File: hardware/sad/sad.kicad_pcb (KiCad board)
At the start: 2 copper layers, 69 parts, among them IC1 LP5012RUKR, J1 USB_C_Receptacle_USB2.0_16P, U1 ATtiny1616-M, U2 MCP73831-2-OT

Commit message: switches updated; border
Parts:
- moved C4 1.90 mm to (158.0, 83.8), turned to -90 degrees
- moved C3 1.84 mm to (147.8, 83.7), turned to -90 degrees
- moved R8 0.90 mm to (158.0, 81.2), turned to 90 degrees
- moved R9 0.90 mm to (147.8, 81.2), turned to 90 degrees
- moved C1 0.79 mm to (168.8, 83.3)
- moved C2 0.79 mm to (167.8, 83.3)
- moved R10 0.79 mm to (174.2, 81.9)
- moved R11 0.79 mm to (174.2, 84.2)
- moved R2 0.79 mm to (169.2, 85.5)
- moved U1 0.79 mm to (171.5, 83.2)
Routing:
- net Net-(S2-NO_1): track 2.17 -> 0.00 mm
- net /SW2: track 1.01 -> 0.00 mm
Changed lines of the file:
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@@
 	(footprint "Resistor_SMD:R_0402_1005Metric_Pad0.72x0.64mm_HandSolder"
 		(layer "F.Cu")
-		(at 158.75 80.75 180)
+		(at 158 81.25 90)
 		(descr "Resistor SMD 0402 (1005 Metric), square (rectangular) end terminal, IPC-7351 nominal with elongated pad for handsoldering. (Body size source: IPC-SM-782 page 72, https://www.pcb-3d.com/wordpress/wp-content/uploads/ipc-sm-782a_amendment_1_and_2.pdf)")
 		(tags "resistor handsolder")
 		(property "Reference" "R8"
-			(at -2 0 0)
+			(at 0 1.5 180)
 			(layer "F.SilkS")
 			(effects
@@
 		)
 		(property "Value" "1k"
-			(at 0 1.17 0)
+			(at 0 1.17 90)
 			(layer "F.Fab")
 			(effects
@@
 		)
 		(property "Datasheet" ""
-			(at 0 0 0)
+			(at 0 0 90)
 			(layer "F.Fab")
 			(hide yes)
@@
 		)
 		(property "Description" "Resistor"
-			(at 0 0 0)
+			(at 0 0 90)
 			(layer "F.Fab")
 			(hide yes)
@@
 		)
 		(property "KiLib_Generator" "SMD_2terminal_chip_molded"
-			(at 0 0 0)
+			(at 0 0 90)
 			(layer "F.SilkS")
 			(hide yes)
@@
 		(duplicate_pad_numbers_are_jumpers no)
 		(fp_line
-			(start -0.167621 0.38)
-			(end 0.167621 0.38)
+			(start -0.167621 -0.38)
+			(end 0.167621 -0.38)
 			(stroke
 				(width 0.12)
@@
 		)
 		(fp_line
-			(start -0.167621 -0.38)
-			(end 0.167621 -0.38)
+			(start -0.167621 0.38)
+			(end 0.167621 0.38)
 			(stroke
 				(width 0.12)
@@
 		)
 		(fp_text user "${REFERENCE}"
-			(at 0 0 0)
+			(at 0 0 90)
 			(layer "F.Fab")
 			(effects
@@
 		)
 		(pad "1" smd roundrect
-			(at -0.5975 0 180)
+			(at -0.5975 0 90)
 			(size 0.715 0.64)
 			(layers "F.Cu" "F.Mask" "F.Paste")
@@
 		)
 		(pad "2" smd roundrect
-			(at 0.5975 0 180)
+			(at 0.5975 0 90)
 			(size 0.715 0.64)
 			(layers "F.Cu" "F.Mask" "F.Paste")
@@
 	(footprint "Capacitor_SMD:C_0402_1005Metric_Pad0.74x0.62mm_HandSolder"
 		(layer "F.Cu")
-		(at 168 83.5675 90)
+		(at 168.75 83.3175 90)
 		(descr "Capacitor SMD 0402 (1005 Metric), square (rectangular) end terminal, IPC-7351 nominal with elongated pad for handsoldering. (Body size source: IPC-SM-782 page 76, https://www.pcb-3d.com/wordpress/wp-content/uploads/ipc-sm-782a_amendment_1_and_2.pdf)")
 		(tags "capacitor handsolder")
@@
 	(footprint "Resistor_SMD:R_0402_1005Metric_Pad0.72x0.64mm_HandSolder"
 		(layer "F.Cu")
-		(at 173.5 82.1525 -90)
+		(at 174.25 81.9025 -90)
 		(descr "Resistor SMD 0402 (1005 Metric), square (rectangular) end terminal, IPC-7351 nominal with elongated pad for handsoldering. (Body size source: IPC-SM-782 page 72, https://www.pcb-3d.com/wordpress/wp-content/uploads/ipc-sm-782a_amendment_1_and_2.pdf)")
 		(tags "resistor handsolder")
@@
 	(footprint "Package_DFN_QFN:VQFN-20-1EP_3x3mm_P0.4mm_EP1.7x1.7mm"
 		(layer "F.Cu")
-		(at 170.75 83.5)
+		(at 171.5 83.25)
 		(descr "VQFN, 20 Pin (http://ww1.microchip.com/downloads/en/DeviceDoc/20%20Lead%20VQFN%203x3x0_9mm_1_7EP%20U2B%20C04-21496a.pdf)")
 		(tags "VQFN NoLead")
@@
 	(footprint "Resistor_SMD:R_0402_1005Metric_Pad0.72x0.64mm_HandSolder"
 		(layer "F.Cu")
-		(at 173.5 84.5 90)
+		(at 174.25 84.25 90)
 		(descr "Resistor SMD 0402 (1005 Metric), square (rectangular) end terminal, IPC-7351 nominal with elongated pad for handsoldering. (Body size source: IPC-SM-782 page 72, https://www.pcb-3d.com/wordpress/wp-content/uploads/ipc-sm-782a_amendment_1_and_2.pdf)")
 		(tags "resistor handsolder")
@@
 	(footprint "Capacitor_SMD:C_0402_1005Metric_Pad0.74x0.62mm_HandSolder"
 		(layer "F.Cu")
-		(at 158.75 82 180)
+		(at 158 83.75 -90)
 		(descr "Capacitor SMD 0402 (1005 Metric), square (rectangular) end terminal, IPC-7351 nominal with elongated pad for handsoldering. (Body size source: IPC-SM-782 page 76, https://www.pcb-3d.com/wordpress/wp-content/uploads/ipc-sm-782a_amendment_1_and_2.pdf)")
 		(tags "capacitor handsolder")
 		(property "Reference" "C4"
-			(at 0.25 -1.25 0)
+			(at 0 -1.25 180)
 			(layer "F.SilkS")
 			(effects
@@
 		)
 		(property "Value" "10nF"
-			(at 0 1.16 0)
+			(at 0 1.16 90)
 			(layer "F.Fab")
 			(effects
@@
 		)
 		(property "Datasheet" ""
-			(at 0 0 0)
+			(at 0 0 90)
 			(layer "F.Fab")
 			(hide yes)
@@
 		)
 		(property "Description" "Unpolarized capacitor"
-			(at 0 0 0)
+			(at 0 0 90)
 			(layer "F.Fab")
 			(hide yes)
@@
 		)
 		(property "KiLib_Generator" "SMD_2terminal_chip_molded"
-			(at 0 0 0)
+			(at 0 0 90)
 			(layer "F.SilkS")
 			(hide yes)
@@
 		)
 		(fp_text user "${REFERENCE}"
-			(at 0 0 0)
+			(at 0 0 90)
 			(layer "F.Fab")
 			(effects
@@
 		)
 		(pad "1" smd roundrect
-			(at -0.5675 0 180)
+			(at -0.5675 0 270)
 			(size 0.735 0.62)
 			(layers "F.Cu" "F.Mask" "F.Paste")
@@
 		)
 		(pad "2" smd roundrect
-			(at 0.5675 0 180)
+			(at 0.5675 0 270)
 			(size 0.735 0.62)
 			(layers "F.Cu" "F.Mask" "F.Paste")
@@
 	(footprint "Resistor_SMD:R_0402_1005Metric_Pad0.72x0.64mm_HandSolder"
 		(layer "F.Cu")
-		(at 148.5 80.75)
+		(at 147.75 81.25 90)
 		(descr "Resistor SMD 0402 (1005 Metric), square (rectangular) end terminal, IPC-7351 nominal with elongated pad for handsoldering. (Body size source: IPC-SM-782 page 72, https://www.pcb-3d.com/wordpress/wp-content/uploads/ipc-sm-782a_amendment_1_and_2.pdf)")
 		(tags "resistor handsolder")
 		(property "Reference" "R9"
-			(at 2 0.25 0)
+			(at 0 1.5 180)
 			(layer "F.SilkS")
 			(effects
@@
 		)
 		(property "Value" "1k"
-			(at 0 1.17 0)
+			(at 0 1.17 90)
 			(layer "F.Fab")
 			(effects
@@
 		)
 		(property "Datasheet" ""
-			(at 0 0 0)
+			(at 0 0 90)
 			(layer "F.Fab")
 			(hide yes)
@@
 		)
 		(property "Description" "Resistor"
-			(at 0 0 0)
+			(at 0 0 90)
 			(layer "F.Fab")
 			(hide yes)
@@
 		)
 		(property "KiLib_Generator" "SMD_2terminal_chip_molded"
-			(at 0 0 0)
+			(at 0 0 90)
 			(layer "F.SilkS")
 			(hide yes)
@@
 		)
 		(fp_text user "${REFERENCE}"
-			(at 0 0 0)
+			(at 0 0 90)
 			(layer "F.Fab")
 			(effects
@@
 		)
 		(pad "1" smd roundrect
-			(at -0.5975 0)
+			(at -0.5975 0 90)
 			(size 0.715 0.64)
 			(layers "F.Cu" "F.Mask" "F.Paste")
@@
 		)
 		(pad "2" smd roundrect
-			(at 0.5975 0)
+			(at 0.5975 0 90)
 			(size 0.715 0.64)
 			(layers "F.Cu" "F.Mask" "F.Paste")
@@
 	(footprint "Capacitor_SMD:C_0402_1005Metric_Pad0.74x0.62mm_HandSolder"
 		(layer "F.Cu")
-		(at 167 83.5675 -90)
+		(at 167.75 83.3175 -90)
 		(descr "Capacitor SMD 0402 (1005 Metric), square (rectangular) end terminal, IPC-7351 nominal with elongated pad for handsoldering. (Body size source: IPC-SM-782 page 76, https://www.pcb-3d.com/wordpress/wp-content/uploads/ipc-sm-782a_amendment_1_and_2.pdf)")
 		(tags "capacitor handsolder")
@@
 	(footprint "Resistor_SMD:R_0402_1005Metric_Pad0.72x0.64mm_HandSolder"
 		(layer "F.Cu")
-		(at 168.4 85.75 180)
+		(at 169.15 85.5 180)
 		(descr "Resistor SMD 0402 (1005 Metric), square (rectangular) end terminal, IPC-7351 nominal with elongated pad for handsoldering. (Body size source: IPC-SM-782 page 72, https://www.pcb-3d.com/wordpress/wp-content/uploads/ipc-sm-782a_amendment_1_and_2.pdf)")
 		(tags "resistor handsolder")
@@
 	(footprint "Capacitor_SMD:C_0402_1005Metric_Pad0.74x0.62mm_HandSolder"
 		(layer "F.Cu")
-		(at 148.5 82)
+		(at 147.75 83.6825 -90)
 		(descr "Capacitor SMD 0402 (1005 Metric), square (rectangular) end terminal, IPC-7351 nominal with elongated pad for handsoldering. (Body size source: IPC-SM-782 page 76, https://www.pcb-3d.com/wordpress/wp-content/uploads/ipc-sm-782a_amendment_1_and_2.pdf)")
 		(tags "capacitor handsolder")
 		(property "Reference" "C3"
-			(at 0 1.25 0)
+			(at -0.1825 -1.5 180)
 			(layer "F.SilkS")
 			(effects
@@
 		)
 		(property "Value" "10nF"
-			(at 0 1.16 0)
+			(at 0 1.16 90)
 			(layer "F.Fab")
 			(effects
@@
 		)
 		(property "Datasheet" ""
-			(at 0 0 0)
+			(at 0 0 90)
 			(layer "F.Fab")
 			(hide yes)
@@
 		)
 		(property "Description" "Unpolarized capacitor"
-			(at 0 0 0)
+			(at 0 0 90)
 			(layer "F.Fab")
 			(hide yes)
@@
 		)
 		(property "KiLib_Generator" "SMD_2terminal_chip_molded"
-			(at 0 0 0)
+			(at 0 0 90)
 			(layer "F.SilkS")
 			(hide yes)
@@
 		(duplicate_pad_numbers_are_jumpers no)
 		(fp_line
-			(start -0.115835 -0.36)
-			(end 0.115835 -0.36)
+			(start -0.115835 0.36)
+			(end 0.115835 0.36)
 			(stroke
 				(width 0.12)
@@
 		)
 		(fp_line
-			(start -0.115835 0.36)
-			(end 0.115835 0.36)
+			(start -0.115835 -0.36)
+			(end 0.115835 -0.36)
 			(stroke
 				(width 0.12)
@@
 		)
 		(fp_text user "${REFERENCE}"
-			(at 0 0 0)
+			(at 0 0 90)
 			(layer "F.Fab")
 			(effects
@@
 		)
 		(pad "1" smd roundrect
-			(at -0.5675 0)
+			(at -0.5675 0 270)
 			(size 0.735 0.62)
 			(layers "F.Cu" "F.Mask" "F.Paste")
@@
 		)
 		(pad "2" smd roundrect
-			(at 0.5675 0)
+			(at 0.5675 0 270)
 			(size 0.735 0.62)
 			(layers "F.Cu" "F.Mask" "F.Paste")
@@
 		)
 		(fill no)
-		(layer "F.SilkS")
+		(layer "Margin")
 	)
-	(segment
-		(start 159.0975 81.72)
-		(end 159.0675 81.75)
-		(width 0.2)
-		(layer "F.Cu")
-		(net "/SW2")
-	)
-	(segment
-		(start 159.0975 80.75)
-		(end 159.0975 81.72)
-		(width 0.2)
-		(layer "F.Cu")
-		(net "/SW2")
-	)
-	(segment
-		(start 157.8525 80.8)
-		(end 157.9025 80.75)
-		(width 0.2)
-		(layer "F.Cu")
-		(net "Net-(S2-NO_1)")
+	(group ""
+		(members "30cc43af-841c-4e06-b69e-9c400d63feec" "77d5c5d5-a0e3-48a3-a708-d74c23b37632"
+			"e6151fd6-45f6-4be3-ab72-9c2ef438c917"
+		)
 	)
-	(segment
-		(start 155.75 80.8)
-		(end 157.8525 80.8)
-		(width 0.2)
-		(layer "F.Cu")
-		(net "Net-(S2-NO_1)")
+	(group ""
+		(members "7cb52aa4-decc-4eac-b2a4-c9e430e85759" "8622e778-5f92-4b7f-a265-3c812fcca718"
+			"c399d736-02d8-4c3c-b0d9-f6df45782c60"
+		)
 	)
 	(group ""

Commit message: third of the way there
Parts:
- BAT_GND1, BAT_VCC1: moved to B.Cu
- moved LED_A0 41.6 mm to (169.8, 89.8), turned to 0 degrees
- moved LED_K0 41.4 mm to (169.6, 81.6), turned to 180 degrees
- moved JP0 37.7 mm to (168.0, 83.4)
- moved LED_A1 35.8 mm to (166.8, 89.8), turned to 0 degrees
- moved LED_K1 35.5 mm to (166.6, 81.6), turned to 180 degrees
- moved JP1 31.7 mm to (165.0, 83.4)
- moved LED_A2 29.9 mm to (163.8, 89.8), turned to 0 degrees
- moved LED_K2 29.7 mm to (163.6, 81.6), turned to 180 degrees
- moved LED_K11 26.6 mm to (136.6, 81.6), turned to 180 degrees
- moved LED_A11 26.4 mm to (136.8, 89.8), turned to 0 degrees
- moved JP2 25.7 mm to (162.0, 83.4)
- moved LED_A3 24.2 mm to (160.8, 89.8), turned to 0 degrees
- moved LED_K3 23.9 mm to (160.6, 81.6), turned to 180 degrees
- moved JP10 22.7 mm to (138.0, 83.4)
- moved C2 21.2 mm to (178.2, 64.8), turned to 180 degrees
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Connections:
- U1 pad 1: /SW1 -> unconnected-(U1-PA2-Pad1)
- U1 pad 15: unconnected-(U1-PC0-Pad15) -> /EN
- U1 pad 6: /EN -> /STAT
- U1 pad 7: /SW2 -> /SW1
- U1 pad 8: /STAT -> /SW2
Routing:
- net VBUS: track 0.00 -> 61.0 mm, vias 0 -> 2
- net GND: track 0.00 -> 23.0 mm, vias 0 -> 6
- net Net-(S2-NO_1): track 0.00 -> 7.12 mm
- net Net-(S1-NO_1): track 0.00 -> 7.06 mm
- net VBAT: track 0.00 -> 4.69 mm, vias 0 -> 2
- net Net-(IC1-OUT9): track 0.00 -> 4.35 mm
- net Net-(IC1-OUT8): track 0.00 -> 4.35 mm
- net Net-(IC1-OUT7): track 0.00 -> 4.35 mm
- net Net-(IC1-OUT6): track 0.00 -> 4.35 mm
- net Net-(IC1-OUT5): track 0.00 -> 4.35 mm
- net Net-(IC1-OUT4): track 0.00 -> 4.35 mm
- net Net-(IC1-OUT3): track 0.00 -> 4.35 mm
- net Net-(IC1-OUT2): track 0.00 -> 4.35 mm
- net Net-(IC1-OUT10): track 0.00 -> 4.35 mm
- net Net-(IC1-OUT1): track 0.00 -> 4.35 mm
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- added copper zone on B.Cu, net GND
- added copper zone on F.Cu, net GND
- added copper zone on B.Cu, net VBAT
- added copper zone on F.Cu, net VBAT
- added copper zone on F.Cu, net VBUS
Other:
- board outline added: 60 x 11 mm

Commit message: foottoprinto
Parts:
- moved TP15 30.2 mm to (175.2, 80.8), turned to 90 degrees
- moved TP13 28.8 mm to (175.2, 84.3), turned to 90 degrees
- moved TP12 27.8 mm to (175.2, 86.0), turned to 90 degrees
- moved TP14 24.4 mm to (175.2, 82.5), turned to 90 degrees
- moved R12 20.8 mm to (174.3, 88.5)
- moved U1 19.6 mm to (171.7, 87.0)
- moved C1 19.6 mm to (171.6, 84.2)
- moved C2 19.6 mm to (171.6, 83.2)
- moved R11 19.0 mm to (155.6, 88.8)
- moved C6 18.8 mm to (153.6, 87.7)
- moved IC1 18.8 mm to (157.3, 86.2)
- moved C5 18.2 mm to (160.6, 87.2), turned to 0 degrees
- moved R10 17.6 mm to (158.2, 89.2), turned to 180 degrees
- moved R1 17.0 mm to (162.9, 87.8), turned to 180 degrees
- moved R2 16.7 mm to (160.6, 88.3)
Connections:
- U1 pad 11: unconnected-(U1-PB3-Pad11) -> /EN
- U1 pad 15: /EN -> unconnected-(U1-PC0-Pad15)
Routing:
- net /SW2: track 1.11 -> 52.3 mm
- net /SW1: track 1.11 -> 47.0 mm
- net /STAT: track 1.34 -> 45.5 mm
- net VBAT: track 4.69 -> 33.5 mm, vias 2 -> 5
- net Net-(IC1-OUT11): track 2.15 -> 21.7 mm, vias 0 -> 1
- net /SDA: track 1.53 -> 18.7 mm
- net Net-(IC1-OUT10): track 4.35 -> 21.0 mm, vias 0 -> 1
- net /SCL: track 2.50 -> 18.3 mm, vias 0 -> 2
- net GND: track 23.0 -> 36.4 mm, vias 6 -> 14
- net Net-(IC1-OUT9): track 4.35 -> 17.6 mm, vias 0 -> 1
- net Net-(IC1-OUT2): track 4.35 -> 16.2 mm, vias 0 -> 1
- net Net-(IC1-OUT0): track 2.20 -> 14.0 mm, vias 0 -> 1
- net /EN: track 3.01 -> 14.2 mm
- net Net-(IC1-OUT1): track 4.35 -> 15.2 mm, vias 0 -> 1
- net Net-(IC1-OUT8): track 4.35 -> 15.0 mm, vias 0 -> 1
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
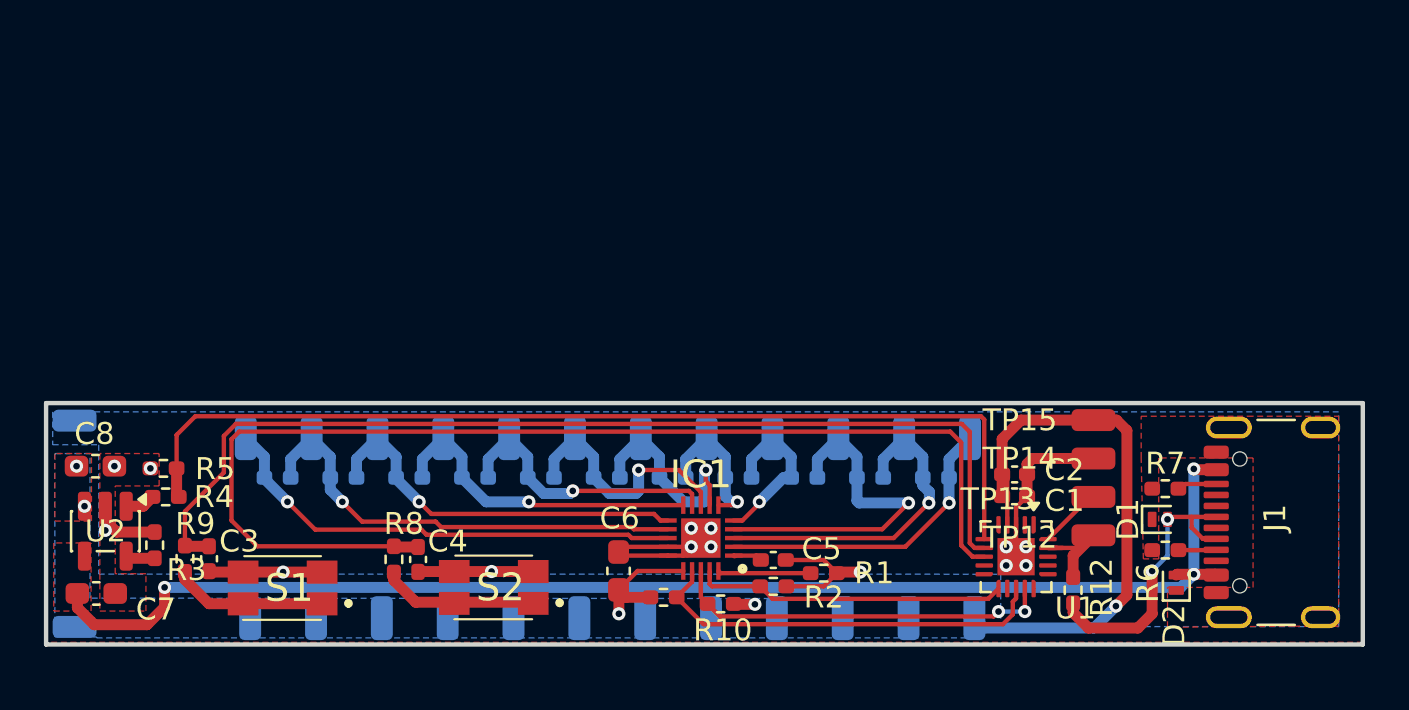
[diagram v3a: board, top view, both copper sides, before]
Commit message: footprint fixes
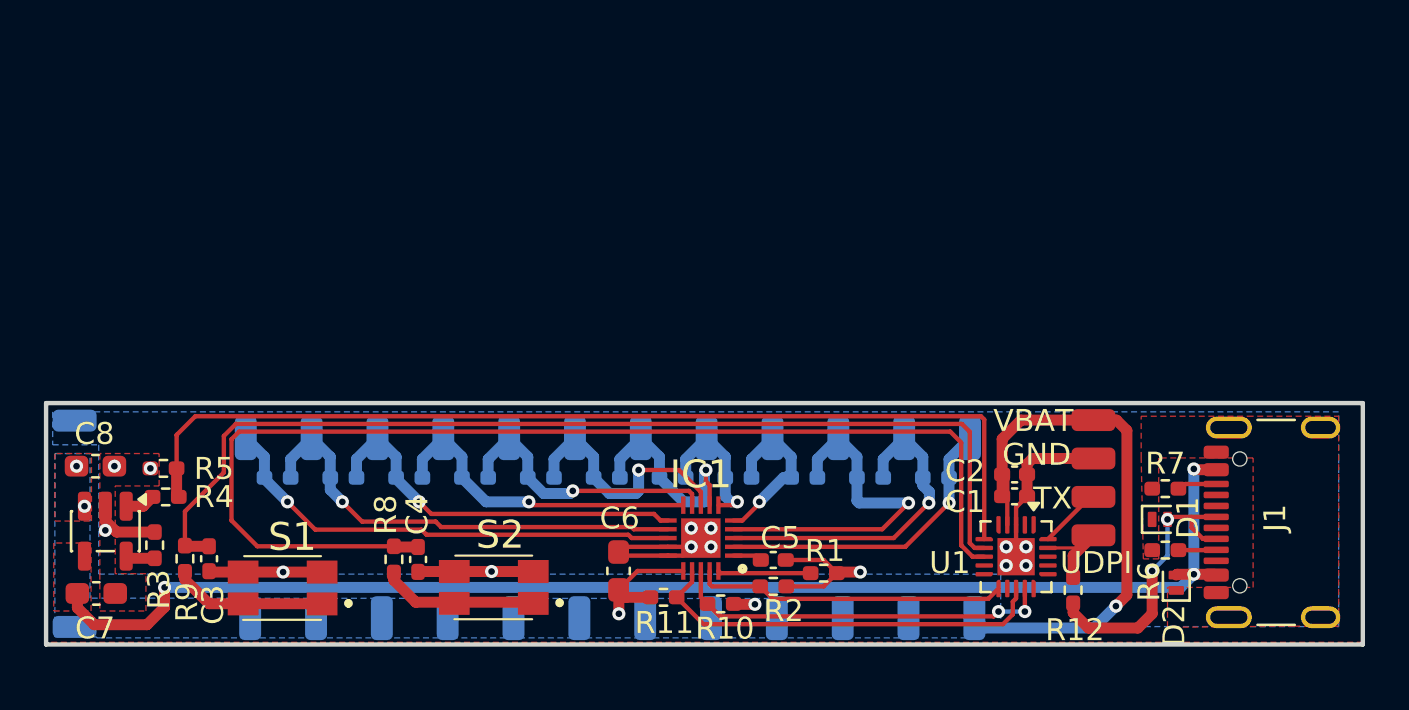
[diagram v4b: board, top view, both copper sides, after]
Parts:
- renumbered TP14 to GND, BAT_GND1 to GND, TP13 to TX, TP12 to UDPI, TP15 to VBAT, BAT_VCC1 to VBAT
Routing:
- net GND: track 36.4 -> 32.8 mm
- net /UDPI: track 5.70 -> 4.60 mm
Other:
- board text added: "A0"
- board text added: "A11"
- board text added: "K0"
- board text added: "K11"
